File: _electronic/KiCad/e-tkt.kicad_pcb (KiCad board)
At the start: 2 copper layers, 99.6 x 76.2 mm, 103 parts, among them J1 USB4105-GF-A, Q1 SS8050-G, Q2 SS8050-G, SW1 B3FS-1000, SW2 B3FS-1000, SW3 B3FS-1000, U1 USB6B1, U2 AZ1117I-3.3, U3 FT231XS, U4 ESP32-WROOM-32, U5 L7806, U6 ULN2003

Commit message: bucket 6v and latch power
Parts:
- removed C17: 0.1uF, Capacitor_SMD:C_0603_1608Metric_Pad1.08x0.95mm_HandSolder
- added 11uH/15.8mOhm1: SRP6060FA-100M, SRP6060FA:SRP6060FA-4R7M, F.Cu at (204.4, -165.6)
- added C18: 22uF, Capacitor_SMD:C_0603_1608Metric_Pad1.08x0.95mm_HandSolder, F.Cu at (140.2, -182.8)
- added C_BST1: 100nF 64mOhm, Capacitor_SMD:C_0603_1608Metric_Pad1.08x0.95mm_HandSolder, F.Cu at (199.1, -172.1)
- added C_FF1: 82pF/0Ohm, Capacitor_SMD:C_0603_1608Metric_Pad1.08x0.95mm_HandSolder, F.Cu at (202.7, -175.7)
- added C_IN1: 10uF/5mOhm, Capacitor_SMD:C_1210_3225Metric_Pad1.33x2.70mm_HandSolder, F.Cu at (210.3, -176.2)
- added C_IN2: 10uF/5mOhm, Capacitor_SMD:C_1210_3225Metric_Pad1.33x2.70mm_HandSolder, F.Cu at (213.9, -176.2)
- added C_IN3: 10uF/5mOhm, Capacitor_SMD:C_1210_3225Metric_Pad1.33x2.70mm_HandSolder, F.Cu at (217.4, -176.2)
- added C_OUT1: 22uF/1mOhm, Capacitor_SMD:C_1210_3225Metric_Pad1.33x2.70mm_HandSolder, F.Cu at (210.3, -164.1)
- added C_OUT2: 22uF/1mOhm, Capacitor_SMD:C_1210_3225Metric_Pad1.33x2.70mm_HandSolder, F.Cu at (213.9, -164.1)
- added C_OUT3: 22uF/1mOhm, Capacitor_SMD:C_1210_3225Metric_Pad1.33x2.70mm_HandSolder, F.Cu at (217.4, -164.1)
- added C_OUT4: 22uF/1mOhm, Capacitor_SMD:C_1210_3225Metric_Pad1.33x2.70mm_HandSolder, F.Cu at (217.4, -170.6)
- added C_OUT5: 22uF/1mOhm, Capacitor_SMD:C_1210_3225Metric_Pad1.33x2.70mm_HandSolder, F.Cu at (213.9, -170.6)
- added D2: LED, LED_SMD:LED_0603_1608Metric_Pad1.05x0.95mm_HandSolder, F.Cu at (141.7, -202.7)
- added Q3: AO3401A, Package_TO_SOT_SMD:SOT-23, F.Cu at (140.2, -177.8)
- added Q4: 2SC4213, Package_TO_SOT_SMD:SOT-23, F.Cu at (145.3, -175.0)
- added Q5: 2SC4213, Package_TO_SOT_SMD:SOT-23, F.Cu at (145.3, -181.9)
- added R28: 430R, Resistor_SMD:R_0603_1608Metric_Pad0.98x0.95mm_HandSolder, F.Cu at (137.9, -202.7)
- added R29: 100K, Resistor_SMD:R_0603_1608Metric_Pad0.98x0.95mm_HandSolder, F.Cu at (145.3, -178.3)
- added R30: 100K, Resistor_SMD:R_0603_1608Metric_Pad0.98x0.95mm_HandSolder, F.Cu at (140.2, -174.5)
- added R31: 1M, Resistor_SMD:R_0603_1608Metric_Pad0.98x0.95mm_HandSolder, F.Cu at (140.2, -181.0)
- added R32: 100K, Resistor_SMD:R_0603_1608Metric_Pad0.98x0.95mm_HandSolder, F.Cu at (148.8, -179.5)
- added R_FBT1: 100K, Resistor_SMD:R_0603_1608Metric_Pad0.98x0.95mm_HandSolder, F.Cu at (204.2, -175.7)
- added R_FFB1: 11K, Resistor_SMD:R_0603_1608Metric_Pad0.98x0.95mm_HandSolder, F.Cu at (201.2, -175.7)
- added SW4: B3FS-1000, b3fs:B3FS-1000, F.Cu at (141.7, -211.8)
- C14: value 0.33uF -> 22uF/1mOhm; footprint Capacitor_SMD:C_0603_1608Metric_Pad1.08x0.95mm_HandSolder -> Capacitor_SMD:C_1210_3225Metric_Pad1.33x2.70mm_HandSolder
- Q_HALL1, Q_SERVO1: footprint Package_TO_SOT_SMD:SOT-323_SC-70 -> Package_TO_SOT_SMD:SOT-23
- R2: footprint Resistor_SMD:R_0603_1608Metric -> Resistor_SMD:R_0603_1608Metric_Pad0.98x0.95mm_HandSolder
- U5: value L7806 -> TPS54302; footprint Package_TO_SOT_SMD:TO-263-2 -> Package_TO_SOT_SMD:SOT-23-6
- moved R2 29.0 mm to (137.9, -204.7), turned to 0 degrees
- moved D11 27.0 mm to (141.7, -204.7), turned to 180 degrees
- moved D_USBIN1 20.4 mm to (141.7, -200.6), turned to 180 degrees
- moved R6 16.6 mm to (137.9, -200.6), turned to 180 degrees
- moved C14 15.4 mm to (198.4, -164.1), turned to 90 degrees
- moved J_OLED1 7.84 mm to (147.8, -208.0), turned to 0 degrees
- moved U5 7.61 mm to (202.7, -171.8), turned to 90 degrees
- moved J_LED_END1 6.66 mm to (156.5, -215.6)
- moved J_LED_PRESS1 6.47 mm to (152.1, -215.6)
- moved R21 6.35 mm to (156.5, -210.6), turned to 180 degrees
- moved R20 6.15 mm to (152.1, -210.6), turned to 180 degrees
- moved R25 4.06 mm to (191.5, -172.7)
- moved D10 4.06 mm to (193.5, -172.7)
- moved Q_SERVO1 4.06 mm to (192.5, -166.4)
- moved R12 4.06 mm to (192.5, -163.3)
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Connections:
- C14 pad 1: +12V -> +6V
- J_LED_END1 pad 1: Net-(J_LED_END1-Pad1) -> GNDREF
- J_LED_END1 pad 2: IO5 LED END -> Net-(J_LED_END1-Pad2)
- J_LED_PRESS1 pad 1: Net-(J_LED_PRESS1-Pad1) -> GNDREF
- J_LED_PRESS1 pad 2: IO17 LED PRESS -> Net-(J_LED_PRESS1-Pad2)
- J_masterpower1 pad 1: +12V -> /POWER IN
- R20 pad 1: Net-(J_LED_PRESS1-Pad1) -> IO17 LED PRESS
- R20 pad 2: GNDREF -> Net-(J_LED_PRESS1-Pad2)
- R21 pad 1: Net-(J_LED_END1-Pad1) -> IO5 LED END
- R21 pad 2: GNDREF -> Net-(J_LED_END1-Pad2)
- U5 pad 1: +12V -> GNDREF
- U5 pad 2: GNDREF -> Net-(C_BST1-Pad2)
- U5 pad 3: +6V -> +12V
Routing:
- net +12V: track 201.7 -> 286.6 mm, vias 9 -> 12
- net Net-(Q4-Pad1): track 0.00 -> 52.3 mm, vias 0 -> 2
- net /POWER IN: track 0.00 -> 50.4 mm, vias 0 -> 2
- net Net-(Q5-Pad3): track 0.00 -> 41.0 mm, vias 0 -> 2
- net GNDREF: track 58.8 -> 23.0 mm, vias 214 -> 238
- net +6V: track 171.5 -> 147.4 mm, vias 4 -> 12
- net IO21 OLED SDA: track 65.6 -> 43.3 mm
- net VBUS: track 25.2 -> 46.8 mm, vias 3 -> 4
- net IO22 OLED SCL: track 58.9 -> 42.7 mm
- net +3.3V: track 303.5 -> 289.5 mm
- net IO17 LED PRESS: track 48.1 -> 40.7 mm, vias 3 -> 2
- net IO5 LED END: track 37.9 -> 31.2 mm
- net Net-(Q3-Pad1): track 0.00 -> 6.02 mm
- net Net-(C_FF1-Pad2): track 0.00 -> 5.18 mm
- net Net-(C18-Pad1): track 0.00 -> 5.13 mm
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- added copper zone on F.Cu, net +12V
- added copper zone on B.Cu, net +6V
- added copper zone on F.Cu, net +6V
- added copper zone on F.Cu, net Net-(C_BST1-Pad2)
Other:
- board text added: "ON"
- board text added: "PWR"
- board text removed: "POWER"

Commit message: added vias, revised parts, fixed schematic
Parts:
- A_NEMA1: renamed from A_DRIVER1; value Pololu_Breakout_A4988 -> 8+8 pin
- C_ENA1: renamed from C4; value 0.1uF/50v(10%) -> 0.1uF 10V
- C_MCU1: renamed from C7; value 0.1uF/50v(10%) -> 0.1uF 10V
- C_MCU2: renamed from C6; value 22uF/10V(20%) -> 22uF 12V 1mOhm
- C_NEMA1: renamed from C8; value 100uF -> 100uF 25V
- C_NEMA2: renamed from C9; value 10uF/25v -> 10uF 12V 5mOhm
- C_POW1: renamed from C10; value 10uF/10V(20%) -> 10uF 12V 5mOhm
- C_POW2: renamed from C11; value 22uF/10V(20%) -> 22uF 12V 1mOhm
- C_POW3: renamed from C18; value 22uF -> 22uF 12V 1mOhm
- C_POW_6V_FF1: renamed from C_FF1; value 82pF/0Ohm -> 82pF 6V 0Ohm
- C_POW_BST1: renamed from C_BST1; value 100nF 64mOhm -> 100nF 6V 64mOhm
- C_POW_IN1: renamed from C_IN1; value 10uF/5mOhm -> 10uF 12V 5mOhm
- C_POW_IN2: renamed from C_IN2; value 10uF/5mOhm -> 10uF 12V 5mOhm
- C_POW_IN3: renamed from C_IN3; value 10uF/5mOhm -> 10uF 12V 5mOhm
- C_POW_OUT1: renamed from C_OUT1; value 22uF/1mOhm -> 22uF 12V 1mOhm
- C_POW_OUT2: renamed from C_OUT2; value 22uF/1mOhm -> 22uF 12V 1mOhm
- C_POW_OUT3: renamed from C_OUT3; value 22uF/1mOhm -> 22uF 12V 1mOhm
- C_POW_OUT4: renamed from C_OUT4; value 22uF/1mOhm -> 22uF 12V 1mOhm
- C_POW_OUT5: renamed from C_OUT5; value 22uF/1mOhm -> 22uF 12V 1mOhm
- C_RST1: renamed from C3; value 0.1uF/50v(10%) -> 0.1uF 10V
- C_SER1: renamed from C16; value 0.1uF -> 0.1uF 10V
- C_SER2: renamed from C5; value 47pF -> 47pF 5V
- C_SER3: renamed from C13; value 47pF -> 47pF 5V
- C_SER4: renamed from C15; value 0.1uF -> 0.1uF 10V
- C_SER5: renamed from C2; value 10uF/25v -> 10uF 12V 5mOhm
- C_SERVO1: renamed from C14; value 22uF/1mOhm -> 22uF 12V 1mOhm
- C_STP1: renamed from C12; value 10uF/25v -> 10uF 12V 5mOhm
- C_WIFI1: renamed from C1; value 0.1uF/50v(10%) -> 0.1uF 10V
- D_HALL1: renamed from D9; value LED -> LED white
- D_NEMA1: renamed from D4; value LED -> LED white
- D_NEMA2: renamed from D1; value LED -> LED white
- D_POW1: renamed from D2; value LED -> LED white
- D_POW2: renamed from D11; value LED -> LED white
- D_RX1, D_TX1: value LED -> LED white
- D_SERVO1: renamed from D10; value LED -> LED white
- D_STP1: renamed from D5; value LED -> LED white
- D_STP2: renamed from D6; value LED -> LED white
- D_STP3: renamed from D7; value LED -> LED white
- D_STP4: renamed from D8; value LED -> LED white
- D_USB1: renamed from D_USBIN1; value LED -> LED white
- FB_USB1: renamed from FB1; value 6V 750mA -> 40 Ohms @ 100 MHz 1 Power
- F_USB1: renamed from F1; value 6V 40A 750mA -> 6V 750mA
- H1, H2, H3, H4, H6: value MountingHole_Pad -> M3
- JP_SER1: renamed from JP5; value SolderJumper_2_Bridged -> Bridged
- JP_SER2: renamed from JP7; value SolderJumper_2_Bridged -> Bridged
- JP_SER3: renamed from JP4; value SolderJumper_2_Bridged -> Bridged
- JP_SER4: renamed from JP6; value SolderJumper_2_Bridged -> Bridged
- J_NEMA1: renamed from J_17HS4023_1; footprint Connector_PinHeader_2.54mm:PinHeader_1x04_P2.54mm_Vertical -> Connector_PinHeader_2.54mm:PinHeader_1x04_P2.54mm_Horizontal
- L1: renamed from 11uH/15.8mOhm1; value SRP6060FA-100M -> 11uH/15.8mOhm1
- Q_AUTO1: renamed from Q1; value SS8050-G -> SS8050
- Q_AUTO2: renamed from Q2; value SS8050-G -> SS8050
- Q_POW1: renamed from Q3; value AO3401A -> ?
- Q_POW2: renamed from Q4; value 2SC4213 -> ?
- Q_POW3: renamed from Q5; value 2SC4213 -> ?
- R_AUTO1: renamed from R7; value 10K(5%) -> 10K (5%); footprint Resistor_SMD:R_0603_1608Metric -> Resistor_SMD:R_0603_1608Metric_Pad0.98x0.95mm_HandSolder
- R_AUTO2: renamed from R8; value 10K(5%) -> 10K (5%); footprint Resistor_SMD:R_0603_1608Metric -> Resistor_SMD:R_0603_1608Metric_Pad0.98x0.95mm_HandSolder
- R_ENA1: renamed from R1; value 10K(5%) -> 10K (5%); footprint Resistor_SMD:R_0603_1608Metric -> Resistor_SMD:R_0603_1608Metric_Pad0.98x0.95mm_HandSolder
- R_HALL1: renamed from R10; value 10K -> 10K (5%); footprint Resistor_SMD:R_0603_1608Metric -> Resistor_SMD:R_0603_1608Metric_Pad0.98x0.95mm_HandSolder
- R_HALL2: renamed from R11; value 10K -> 10K (5%); footprint Resistor_SMD:R_0603_1608Metric -> Resistor_SMD:R_0603_1608Metric_Pad0.98x0.95mm_HandSolder
- R_HALL3: renamed from R24; value 47R -> 27R; footprint Resistor_SMD:R_0603_1608Metric -> Resistor_SMD:R_0603_1608Metric_Pad0.98x0.95mm_HandSolder
- R_LEDE1: renamed from R21; value 47R -> 27R; footprint Resistor_SMD:R_0603_1608Metric -> Resistor_SMD:R_0603_1608Metric_Pad0.98x0.95mm_HandSolder
- R_LEDP1: renamed from R20; value 47R -> 27R; footprint Resistor_SMD:R_0603_1608Metric -> Resistor_SMD:R_0603_1608Metric_Pad0.98x0.95mm_HandSolder
- R_NEMA1: renamed from R26; value 47R -> 27R; footprint Resistor_SMD:R_0603_1608Metric -> Resistor_SMD:R_0603_1608Metric_Pad0.98x0.95mm_HandSolder
- R_NEMA2: renamed from R27; value 47R -> 27R; footprint Resistor_SMD:R_0603_1608Metric -> Resistor_SMD:R_0603_1608Metric_Pad0.98x0.95mm_HandSolder
- R_RST1: renamed from R5; value 10K(5%) -> 10K (5%); footprint Resistor_SMD:R_0603_1608Metric -> Resistor_SMD:R_0603_1608Metric_Pad0.98x0.95mm_HandSolder
- R_RX1: renamed from R22; value 47R -> 27R; footprint Resistor_SMD:R_0603_1608Metric -> Resistor_SMD:R_0603_1608Metric_Pad0.98x0.95mm_HandSolder
- R_SERVO1: renamed from R12; value 10K -> 10K (5%); footprint Resistor_SMD:R_0603_1608Metric -> Resistor_SMD:R_0603_1608Metric_Pad0.98x0.95mm_HandSolder
- R_SERVO2: renamed from R13; value 10K -> 10K (5%); footprint Resistor_SMD:R_0603_1608Metric -> Resistor_SMD:R_0603_1608Metric_Pad0.98x0.95mm_HandSolder
- R_SERVO3: renamed from R25; value 47R -> 27R; footprint Resistor_SMD:R_0603_1608Metric -> Resistor_SMD:R_0603_1608Metric_Pad0.98x0.95mm_HandSolder
- R_STP1: renamed from R15; footprint Resistor_SMD:R_0603_1608Metric -> Resistor_SMD:R_0603_1608Metric_Pad0.98x0.95mm_HandSolder
- R_STP2: renamed from R16; footprint Resistor_SMD:R_0603_1608Metric -> Resistor_SMD:R_0603_1608Metric_Pad0.98x0.95mm_HandSolder
- R_STP3: renamed from R17; footprint Resistor_SMD:R_0603_1608Metric -> Resistor_SMD:R_0603_1608Metric_Pad0.98x0.95mm_HandSolder
- R_STP4: renamed from R18; footprint Resistor_SMD:R_0603_1608Metric -> Resistor_SMD:R_0603_1608Metric_Pad0.98x0.95mm_HandSolder
- R_TX1: renamed from R23; value 47R -> 27R; footprint Resistor_SMD:R_0603_1608Metric -> Resistor_SMD:R_0603_1608Metric_Pad0.98x0.95mm_HandSolder
- R_USB1: renamed from R3; value 5.1K(10%) -> 5.1K (10%)
- R_USB2: renamed from R9; value 5.1K(10%) -> 5.1K (10%)
- U_POW2: renamed from U2; value AZ1117I-3.3 -> AZ1117CH-3.3TRG1
- U_SER1: renamed from U3; value FT231XS -> FT231XS-R
- moved C_POW1 1.32 mm to (198.8, -183.9)
- moved U_POW2 1.32 mm to (201.1, -189.5)
- moved C_POW_BST1 1.27 mm to (200.4, -172.1)
- moved C_POW_IN2 1.27 mm to (215.1, -176.2)
- moved C_POW_OUT2 1.27 mm to (215.1, -164.1)
- moved C_POW_OUT5 1.27 mm to (215.1, -170.6)
- moved L1 1.27 mm to (205.7, -165.6)
- moved C_POW_IN1 1.27 mm to (211.6, -176.2)
- moved C_POW_IN3 1.27 mm to (218.7, -176.2)
- moved C_POW_OUT1 1.27 mm to (211.6, -164.1)
- moved C_POW_OUT3 1.27 mm to (218.7, -164.1)
- moved C_POW_OUT4 1.27 mm to (218.7, -170.6)
- moved U_POW1 1.27 mm to (204.0, -171.8)
- moved SW_POW1 1.26 mm to (140.5, -211.8)
- moved SW_ENA1 1.04 mm to (200.9, -211.8)
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- renumbered J_LED_END1 to J_LEDE1, J_LED_PRESS1 to J_LEDP1, J_masterpower1 to J_POW1, J1 to J_USB1, R28 to R_POW1, R29 to R_POW2, R30 to R_POW3, R31 to R_POW4, R32 to R_POW5, R2 to R_POW6, R_FBT1 to R_POW_FBT1, R_FFB1 to R_POW_FFB1, R14 to R_SER1, R19 to R_SER2, R6 to R_USB3, R4 to R_WIFI1, SW2 to SW_ENA1, SW4 to SW_POW1, SW1 to SW_RST1, SW3 to SW_WIFI1, U4 to U_MCU1, U5 to U_POW1, U6 to U_STP1, U1 to U_USB1
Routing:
- net /POWER IN: track 50.4 -> 36.5 mm
- net GNDREF: track 23.0 -> 17.9 mm, vias 238 -> 598
- net Net-(Q_POW3-Pad3): track 41.0 -> 44.2 mm
- net IO32 NEMA STEP: track 50.3 -> 47.6 mm
- net IO33 NEMA DIR: track 49.0 -> 46.5 mm
- net +3.3V: track 289.5 -> 292.0 mm
- net IO14 SERVO: track 71.1 -> 69.2 mm
- net +12V: track 286.6 -> 285.3 mm
- net Net-(Q_POW2-Pad1): track 52.3 -> 53.4 mm
- net +6V: track 147.4 -> 148.3 mm, vias 12 -> 18
- net EN: track 53.3 -> 54.2 mm
- net Net-(D_RX1-Pad1): track 2.05 -> 2.77 mm
- net Net-(D_TX1-Pad1): track 2.05 -> 2.77 mm
- net Net-(C_POW_6V_FF1-Pad2): track 5.18 -> 4.46 mm
- added copper zone on F.Cu, net /POWER IN
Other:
- outline, holes or cut-outs redrawn
- board text added: "+"
- board text added: "12V 3A"
- board text added: "2022/07/18"
- board text added: "WIFI"
- board text removed: "+WIFI"
- board text removed: "12v 3A"
- board text removed: "2022/07/09"

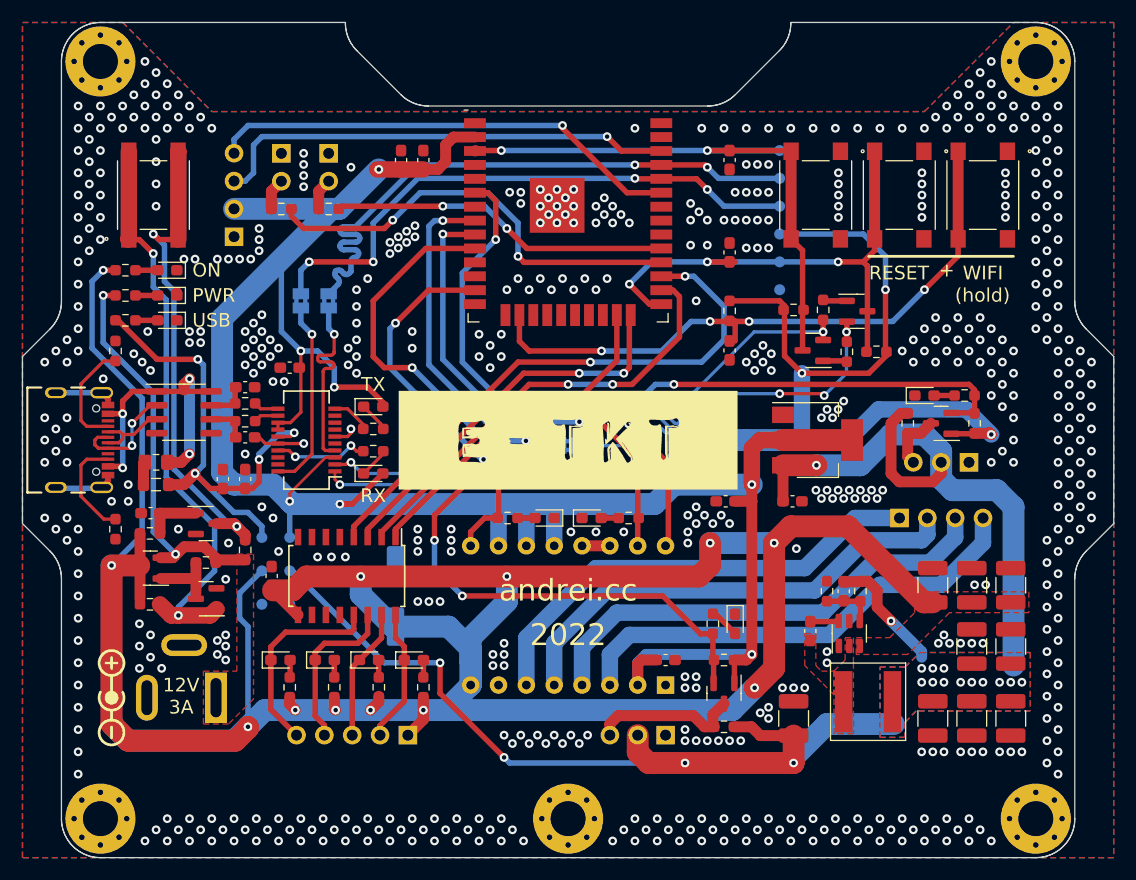
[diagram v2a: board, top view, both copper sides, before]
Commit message: visual identity on silk and exposed copper layers
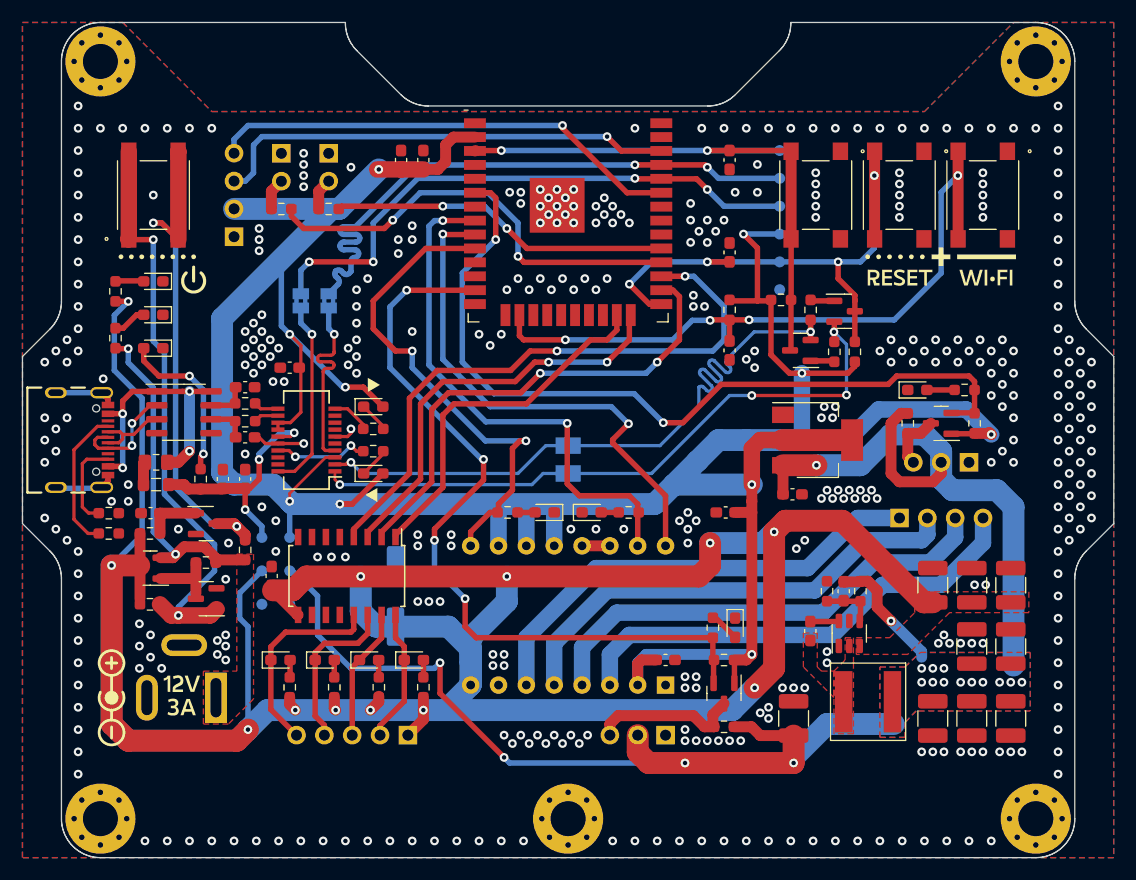
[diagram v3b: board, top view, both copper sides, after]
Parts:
- added G*** (x3): LOGO, LOGO, F.Cu at (178.3, -189.5)
- added REF**: OSHW-Symbol_6.7x6mm_SilkScreen, Symbol:OSHW-Symbol_6.7x6mm_SilkScreen, B.Cu at (212.3, -209.0)
- J_HALL1: value Conn_01x03_Male -> Conn_01x03_Female; footprint Connector_PinHeader_2.54mm:PinHeader_1x03_P2.54mm_Vertical -> Connector_PinSocket_2.54mm:PinSocket_1x03_P2.54mm_Vertical
- Q_POW1: value ? -> IRLML6302TRPBF
- Q_POW2, Q_POW3: value ? -> MMBT3904,215
- moved R_USB1 16.7 mm to (136.4, -181.0), turned to 180 degrees
- moved R_USB3 16.0 mm to (144.8, -185.9), turned to -90 degrees
- moved R_POW1 4.00 mm to (137.0, -198.8), turned to 90 degrees
- moved D_USB1 2.84 mm to (140.5, -197.9)
- moved D_POW1 2.17 mm to (140.5, -200.9)
- moved R_POW6 2.13 mm to (137.0, -203.0), turned to 90 degrees
- moved R_RST1 1.97 mm to (204.5, -197.5), turned to 90 degrees
- moved D_POW2 1.63 mm to (140.5, -204.0)
- moved R_USB2 1.58 mm to (136.4, -182.8), turned to 180 degrees
- moved R_ENA1 1.46 mm to (197.7, -202.3)
- moved Q_AUTO1 1.14 mm to (199.5, -197.7)
- moved Q_AUTO2 1.14 mm to (203.5, -201.2)
- moved R_AUTO1 1.14 mm to (202.6, -197.5)
- moved R_AUTO2 1.14 mm to (200.4, -201.4)
- moved C_POW2 1.02 mm to (192.7, -182.9)
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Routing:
- net VBUS: track 46.8 -> 21.8 mm, vias 4 -> 3
- net Net-(D_USB1-Pad2): track 2.02 -> 15.0 mm, vias 0 -> 2
- net +3.3V: track 292.0 -> 280.1 mm
- net /POWER IN: track 36.5 -> 30.7 mm
- net IO0 RESET: track 47.4 -> 52.2 mm, vias 3 -> 4
- net IO13 WIFI RST: track 57.8 -> 62.5 mm
- net IO4 ULN 2: track 40.6 -> 44.6 mm
- net IO16 ULN 4: track 51.7 -> 55.6 mm
- net IO34 HALL: track 70.9 -> 74.4 mm
- net Net-(J_USB1-PadA5): track 10.1 -> 13.1 mm
- net Net-(Q_POW3-Pad3): track 44.2 -> 47.0 mm
- net Net-(F_USB1-Pad1): track 27.7 -> 25.2 mm
- net IO14 SERVO: track 69.2 -> 71.6 mm
- net IO2 ULN 3: track 35.6 -> 37.9 mm
- net IO15 ULN 1: track 31.4 -> 33.4 mm
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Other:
- board text removed: "(hold)"
- board text removed: "+"
- board text removed: "12V 3A"
- board text removed: "2022"
- board text removed: "Andrei Speridião"
- board text removed: "ON"
- board text removed: "PWR"
- board text removed: "RESET"
- board text removed: "USB"
- board text removed: "WIFI"
- board text removed: "andrei.cc"
- board text removed: "github.com/andreisperid/E-TKT"
